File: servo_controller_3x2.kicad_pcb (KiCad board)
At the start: 2 copper layers, 70.5 x 41.9 mm, 1 part

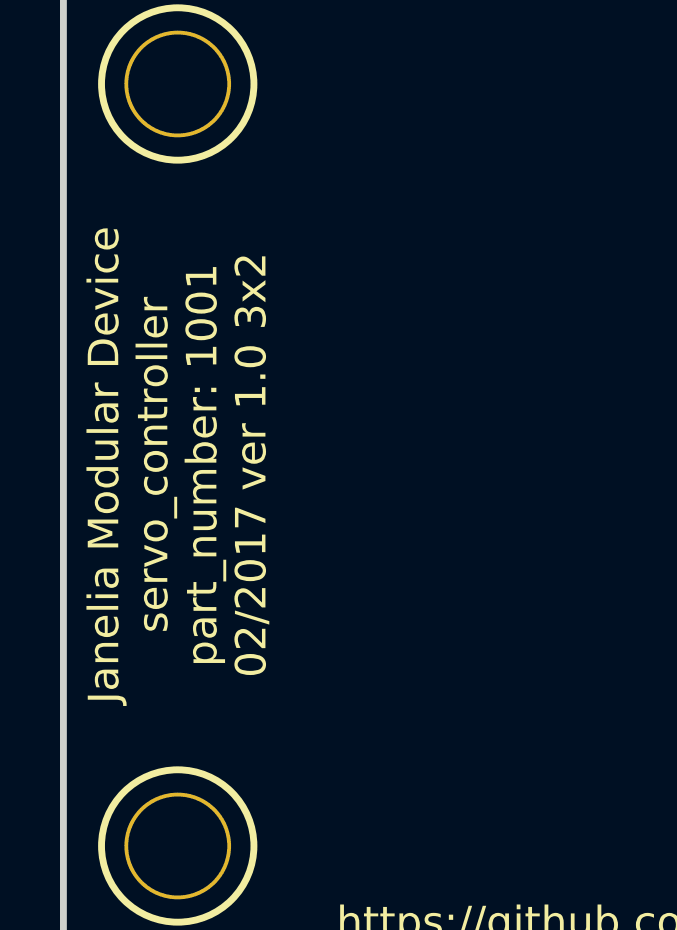
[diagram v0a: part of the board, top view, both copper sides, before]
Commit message: Added components.
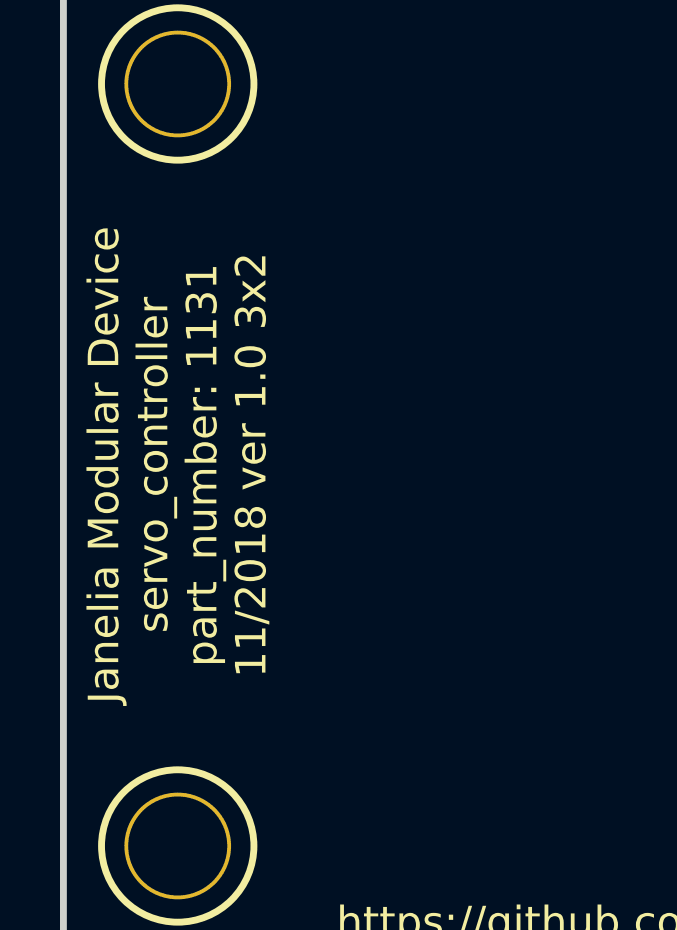
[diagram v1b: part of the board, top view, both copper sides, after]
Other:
- board text added: "Janelia Modular Device servo_controller part_number: 1131 11/2018 ver 1.0 3x2"
- board text removed: "Janelia Modular Device servo_controller part_number: 1001 02/2017 ver 1.0 3x2"
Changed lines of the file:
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@@
-(kicad_pcb (version 20170123) (host pcbnew no-vcs-found-0633d90~59~ubuntu16.04.1)
+(kicad_pcb (version 20171130) (host pcbnew 6.0.0-rc1-unknown-4d73cfb~66~ubuntu18.04.1)
   (general
     (thickness 1.6)
@@
     (zone_45_only no)
     (trace_min 0.254)
-    (segment_width 0.2286)
-    (edge_width 0.2286)
     (via_size 0.889)
     (via_drill 0.635)
@@
     (uvia_min_size 0.508)
     (uvia_min_drill 0.127)
+    (edge_width 0.2286)
+    (segment_width 0.2286)
     (pcb_text_width 0.3)
     (pcb_text_size 1.5 1.5)
@@
     (pad_drill 0)
     (pad_to_mask_clearance 0)
+    (solder_mask_min_width 0.25)
     (aux_axis_origin 0 0)
     (visible_elements FFFFF77F)
@@
       (layerselection 0x000f0_ffffffff)
       (usegerberextensions true)
+      (usegerberattributes false)
+      (usegerberadvancedattributes false)
+      (creategerberjobfile false)
       (excludeedgelayer false)
       (linewidth 0.100000)
@@
       (hpglpennumber 1)
       (hpglpenspeed 20)
-      (hpglpendiameter 15)
+      (hpglpendiameter 15.000000)
       (psnegative false)
       (psa4output false)
@@
       (drillshape 0)
       (scaleselection 1)
-      (outputdirectory gerbers/))
+      (outputdirectory "gerbers/"))
   )
   (net 0 "")
@@
     (uvia_dia 0.508)
     (uvia_drill 0.127)
-    (diff_pair_gap 0.254)
-    (diff_pair_width 0.254)
+    (diff_pair_width 0.254)
+    (diff_pair_gap 0.254)
   )
   (net_class GND ""
@@
     (uvia_dia 0.508)
     (uvia_drill 0.127)
-    (diff_pair_gap 0.254)
-    (diff_pair_width 0.254)
+    (diff_pair_width 0.254)
+    (diff_pair_gap 0.254)
   )
   (net_class LEDPOWER ""
@@
     (uvia_dia 0.508)
     (uvia_drill 0.127)
-    (diff_pair_gap 0.254)
-    (diff_pair_width 0.254)
+    (diff_pair_width 0.254)
+    (diff_pair_gap 0.254)
   )
   (net_class POWER ""
@@
     (uvia_dia 0.508)
     (uvia_drill 0.127)
-    (diff_pair_gap 0.254)
-    (diff_pair_width 0.254)
+    (diff_pair_width 0.254)
+    (diff_pair_gap 0.254)
   )
   (net_class SIGNAL ""
@@
     (uvia_dia 0.508)
     (uvia_drill 0.127)
-    (diff_pair_gap 0.254)
-    (diff_pair_width 0.254)
+    (diff_pair_width 0.254)
+    (diff_pair_gap 0.254)
   )
   (net_class SUPERPOWER ""
@@
     (uvia_dia 0.508)
     (uvia_drill 0.127)
-    (diff_pair_gap 0.254)
-    (diff_pair_width 0.254)
+    (diff_pair_width 0.254)
+    (diff_pair_gap 0.254)
   )
   (module servo_controller_3x2:MODULAR_DEVICE_BASE_3X2_MALE (layer F.Cu)
@@
     )
     (fp_text value MODULAR_DEVICE_BASE_3X2_MALE (at 0 2.54) (layer F.SilkS) hide
-      (effects (font (thickness 0.3048)))
+      (effects (font (size 1.524 1.524) (thickness 0.3048)))
     )
     (fp_line (start 48.895 -20.955) (end -21.59 -20.955) (layer F.Fab) (width 0.2286))
@@
     (effects (font (size 1.016 1.016) (thickness 0.1905)))
   )
-  (gr_text "Janelia Modular Device\nservo_controller\npart_number: 1001\n02/2017 ver 1.0 3x2" (at 89.535 88.9 90) (layer F.SilkS)
+  (gr_text "Janelia Modular Device\nservo_controller\npart_number: 1131\n11/2018 ver 1.0 3x2" (at 89.535 88.9 90) (layer F.SilkS)
     (effects (font (size 1.016 1.016) (thickness 0.254)))
   )

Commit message: Progress towards v1.0.
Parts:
- added C1: 220uF_POL, servo_controller_3x2:C_ELEC_10, F.Cu at (148.0, 74.9)
- added C2: 0.1uF, servo_controller_3x2:SM1210, B.Cu at (117.5, 85.1)
- added C3: 10uF, servo_controller_3x2:SM1210, B.Cu at (117.5, 88.3)
- added D1: diode_schottky_45V_10A, servo_controller_3x2:CFP15, B.Cu at (91.4, 93.3)
- added L1: LED_5V_RED, servo_controller_3x2:LED_555-3XXX_R, F.Cu at (144.8, 95.2)
- added P1: PWR_JACK_2.1x5.5, footprints:DCJACK_2PIN_HIGHCURRENT, F.Cu at (156.2, 88.9)
- added P2: HEADER_03X16, servo_controller_3x2:HEADER_03x16, F.Cu at (117.5, 94.0)
- added R1: 4.7k, servo_controller_3x2:SM1210, B.Cu at (112.4, 101.0)
- added R2: 4.7k, servo_controller_3x2:SM1210, B.Cu at (108.0, 101.0)
- added RP1: 220x4, servo_controller_3x2:RESISTOR_PACK_SM1206x4, B.Cu at (132.7, 86.4)
- added RP2: 220x4, servo_controller_3x2:RESISTOR_PACK_SM1206x4, B.Cu at (125.1, 86.4)
- added RP3: 220x4, servo_controller_3x2:RESISTOR_PACK_SM1206x4, B.Cu at (109.9, 86.4)
- added RP4: 220x4, servo_controller_3x2:RESISTOR_PACK_SM1206x4, B.Cu at (102.2, 86.4)
- added U1: PCA9685, servo_controller_3x2:TSSOP28, B.Cu at (117.5, 78.1)
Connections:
- MDB1 pad 18: (no net) -> /SDA
- MDB1 pad 19: (no net) -> /SCL
- MDB1 pad 2: (no net) -> /~ENABLE
- MDB1 pad GND: (no net) -> GND
- MDB1 pad VEE: (no net) -> VEE
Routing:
- net GND: track 0.00 -> 77.7 mm
- net VCC: track 0.00 -> 76.1 mm
- net VEE: track 0.00 -> 14.2 mm
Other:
- net class SUPERPOWER: via_dia 0.889 -> 1.2192

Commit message: Finished routing.
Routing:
- net /SCL: track 0.00 -> 82.0 mm
- net VEE: track 14.2 -> 83.9 mm
- net GND: track 77.7 -> 146.9 mm
- net /SDA: track 0.00 -> 55.5 mm, vias 0 -> 1
- net /~ENABLE: track 0.00 -> 19.1 mm
- net /servo_3x2/PWM_0: track 0.00 -> 17.9 mm
- net /servo_3x2/PWM_15: track 0.00 -> 17.6 mm
- net /servo_3x2/PWM_1: track 0.00 -> 16.3 mm
- net /servo_3x2/PWM_14: track 0.00 -> 16.1 mm
- net /servo_3x2/PWM_2: track 0.00 -> 14.8 mm
- net /servo_3x2/PWM_13: track 0.00 -> 14.5 mm
- net /servo_3x2/PWM_3: track 0.00 -> 13.2 mm
- net /servo_3x2/PWM_12: track 0.00 -> 13.0 mm
- net /servo_3x2/PWM_4: track 0.00 -> 9.17 mm
- net /servo_3x2/PWM_11: track 0.00 -> 8.90 mm
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- added copper zone on B.Cu, net GND
- added copper zone on F.Cu, net VCC
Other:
- net class LOWPOWER added: clearance 0.1016, trace_width 0.4064, via_dia 0.889, via_drill 0.635

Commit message: Finished v1.0.
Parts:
- MDB1: value MODULAR_DEVICE_BASE_3X2_MALE -> VAL**
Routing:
- net /SDA: track 55.5 -> 59.2 mm
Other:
- rule solder_mask_min_width: 0.25 -> 0.1016
- board text added: "2.1x5.5 Center +"
- board text added: "5V"
